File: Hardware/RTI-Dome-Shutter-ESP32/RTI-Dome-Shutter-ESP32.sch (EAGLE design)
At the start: 100 parts, among them IC1 REG1117FA-5.0_500, IC2 24LC64T-I/SN, IC8 REG1117-3.3V, J2 XT60PW-M, T1 MMBT3904LT1, T2 MMBT3904LT1, T3 MMBT3904LT1, U1 W5500, U2 ESP32-DevKitC ESP32-WROOM-32U, X9 J1011F01PNL

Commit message: Adding ESP32 version of the shutter controller
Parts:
- removed 25MHZ: CB3LV-OSCILATOR, rti:CB3LV-OSCILATOR
- removed C10: 22nF, rcl:C-EUC0603
- removed C11, C12, C14, C16, C17, C20: 100nF, rcl:C-EUC0603
- removed C13, C18, C22: 10nF, rcl:C-EUC0603
- removed C15, C21: 6.8nF, rcl:C-EUC0603
- removed C19: 4.7uF, rcl:C-EUC0603
- removed FL1: BLM21AG121SN1D, BLM21AG121SN1D:BLM21AG121SN1D
- removed R23: 10 1%, rcl:R-EU_R0603
- removed R24, R25, R26, R27: 49.9 1%, rcl:R-EU_R0603
- removed R28, R29: 330, rcl:R-EU_R0603
- removed R30, R31, R32, R33, R34, R35, R36, R37, R38, R40: 4.7K, rcl:R-EU_R0603
- removed R39: 12.4K 1%, rcl:R-EU_R0603
- removed U1: W5500, W5500:W5500
- removed X9: J1011F01PNL, rti:J1011F01PNL
- C1, C23, C24, C27, C28, C3, C4, C40, C41, C42, C43, C44, C45, C46, C5, C6: device rcl:C-EUC0603 -> rti:C-EU'0603'
- IC2: device Microchip_By_element14_Batch_1:24LC64T-I/SN -> rti:24LC64T-I/SN
- R1, R10, R12, R15, R16, R17, R18, R2, R20, R21, R22, R3, R4, R41, R44, R45, R46, R47, R48, R49, R5, R50, R6, R7, R8, R9: device rcl:R-EU_R0603 -> rti:R-EU'0603'
- T1, T2, T3: value MMBT3904LT1 -> (none); device samacsys:MMBT3904LT1 -> transistor:MMBT3904LT1-NPN-SOT23-BEC
- U2: value ESP32-DevKitC ESP32-WROOM-32U -> ESP32-DevKitC ESP32-WROOM-32D
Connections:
- removed net ACT_LED: U1.ACTLED, X9.C-L
- removed net AVDD: C11.1, C12.1, C14.1, C17.1, FL1.1, R23.2, R24.2, R25.2, U1.AVDD@1, U1.AVDD@2, U1.AVDD@3, U1.AVDD@4, U1.AVDD@5, U1.AVDD@6
- removed net LINK_ACK: U1.LINKLED, X9.C-R
- removed net N$10: R28.1, X9.AL
- removed net N$11: C15.2, X9.RD+
- removed net N$12: C21.2, X9.RD-
- removed net N$13: C10.1, R23.1, X9.CT
- removed net N$17: U1.DUPLED
- removed net N$22: R31.1, U1.RSVD@2
- removed net N$23: R32.1, U1.RSVD@3
- removed net N$24: R33.1, U1.RSVD@4
- removed net N$25: R34.1, U1.RSVD@5
- removed net N$26: R35.1, U1.RSVD@6
- removed net N$27: R36.1, U1.PMODE2
- removed net N$28: R37.1, U1.PMODE1
- removed net N$29: R38.1, U1.PMODE0
- removed net N$31: C19.2, U1.TOCAP
- removed net N$32: U1.VBG
- removed net N$33: C18.2, U1.1V2O
- removed net N$34: R39.1, U1.EXRES1
- removed net N$35: R40.2, U1.RSVD@1
- removed net N$7: C22.1, R26.2, R27.2, X9.CR
- removed net N$8: R29.1, X9.A-R
- removed net RXN: C21.1, R26.1, U1.RXN
- removed net RXP: C15.1, R27.1, U1.RXP
- removed net TXN: R25.1, U1.TXN, X9.TD-
- removed net TXP: R24.1, U1.TXP, X9.TD+
- removed net XI: 25MHZ.FO, U1.XI/CLKIN
- removed net XO: U1.XO
- net 3.3V: no longer 25MHZ.OE, 25MHZ.VDD, C13.1, C16.1, C20.1, FL1.2, R28.2, R29.2, R30.2, R36.2, R37.2, R38.2, U1.VDD
- net ETH_CS: no longer U1.SCS_N
- net ETH_RESET: no longer R30.1, U1.RST_N
- net GND: no longer 25MHZ.GND, C10.2, C11.2, C12.2, C13.2, C14.2, C16.2, C17.2, C18.1, C19.1, C20.2, C22.2, R31.2, R32.2, R33.2, R34.2, R35.2, R39.2, R40.1, U1.AGND@1, U1.AGND@2, U1.AGND@3, U1.AGND@4, U1.AGND@5, U1.AGND@6, U1.GND, X9.4/NC, X9.5/NC, X9.CGND, X9.CGND2
- net INT_N: no longer U1.INT_N
- net SCLK: no longer U1.SCLK
- net SDI: no longer U1.MISO
- net SDO: no longer U1.MOSI

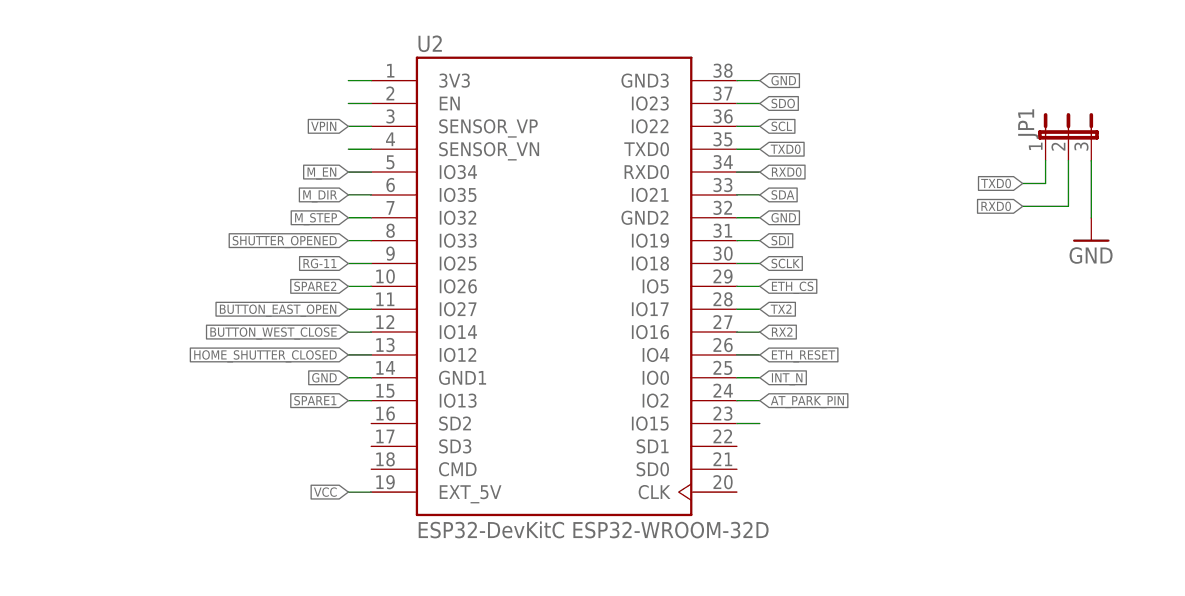
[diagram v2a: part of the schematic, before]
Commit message: Fixed a lot of issue with the ESP32 and serial ports.
Alpaca Discovery and API server are now running in their own tasks.
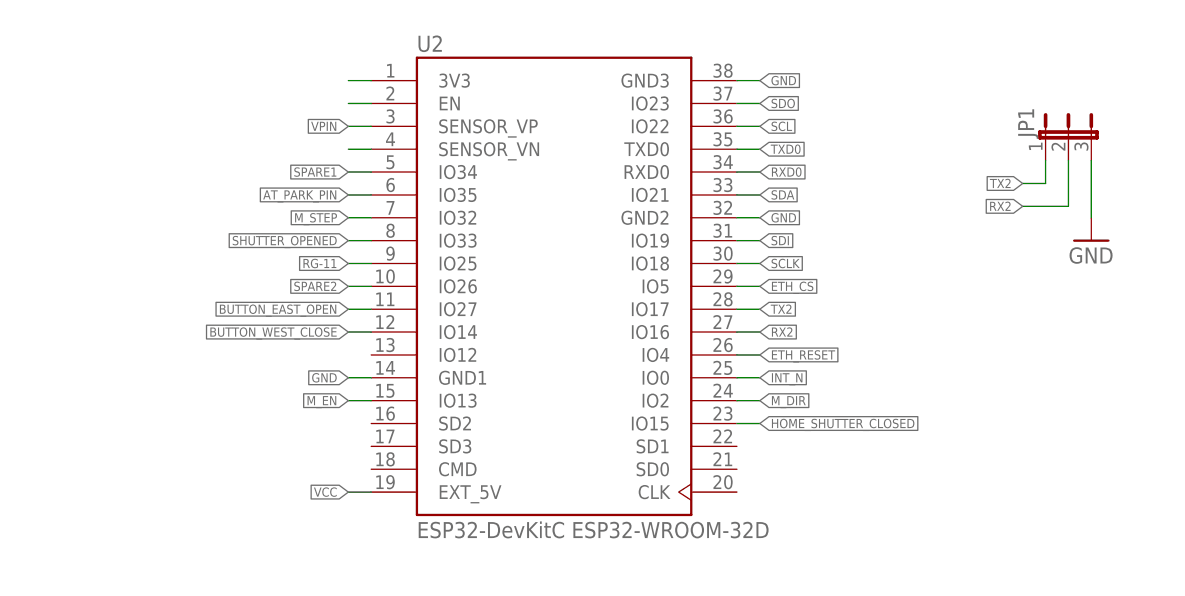
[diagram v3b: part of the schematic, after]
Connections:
- removed net N$15: U2.IO15
- net AT_PARK_PIN: now also U2.IO35; no longer U2.IO2
- net HOME_SHUTTER_CLOSED: now also U2.IO15; no longer U2.IO12
- net M_DIR: now also U2.IO2; no longer U2.IO35
- net M_EN: now also U2.IO13; no longer U2.IO34
- net RX2: now also JP1.2
- net RXD0: no longer JP1.2
- net SPARE1: now also U2.IO34; no longer U2.IO13
- net TX2: now also JP1.1
- net TXD0: no longer JP1.1
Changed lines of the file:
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@@
 </segment>
 <segment>
-<pinref part="U2" gate="G$1" pin="IO34"/>
-<wire x1="80.01" y1="67.31" x2="82.55" y2="67.31" width="0.1524" layer="91"/>
-<label x="80.01" y="67.31" size="1.016" layer="95" rot="R180" xref="yes"/>
+<wire x1="80.01" y1="41.91" x2="82.55" y2="41.91" width="0.1524" layer="91"/>
+<label x="80.01" y="41.91" size="1.016" layer="95" rot="R180" xref="yes"/>
+<pinref part="U2" gate="G$1" pin="IO13"/>
 </segment>
 </net>
@@
 </segment>
 <segment>
-<pinref part="U2" gate="G$1" pin="IO35"/>
-<wire x1="80.01" y1="64.77" x2="82.55" y2="64.77" width="0.1524" layer="91"/>
-<label x="80.01" y="64.77" size="1.016" layer="95" rot="R180" xref="yes"/>
+<wire x1="125.73" y1="41.91" x2="123.19" y2="41.91" width="0.1524" layer="91"/>
+<label x="125.73" y="41.91" size="1.016" layer="95" xref="yes"/>
+<pinref part="U2" gate="G$1" pin="IO2"/>
 </segment>
 </net>
@@
 </segment>
 <segment>
-<wire x1="80.01" y1="46.99" x2="82.55" y2="46.99" width="0.1524" layer="91"/>
-<label x="80.01" y="46.99" size="1.016" layer="95" rot="R180" xref="yes"/>
-<pinref part="U2" gate="G$1" pin="IO12"/>
+<pinref part="U2" gate="G$1" pin="IO15"/>
+<wire x1="125.73" y1="39.37" x2="123.19" y2="39.37" width="0.1524" layer="91"/>
+<label x="125.73" y="39.37" size="1.016" layer="95" xref="yes"/>
 </segment>
 </net>
@@
 </segment>
 <segment>
-<wire x1="125.73" y1="41.91" x2="123.19" y2="41.91" width="0.1524" layer="91"/>
-<label x="125.73" y="41.91" size="1.016" layer="95" xref="yes"/>
-<pinref part="U2" gate="G$1" pin="IO2"/>
+<pinref part="U2" gate="G$1" pin="IO35"/>
+<wire x1="80.01" y1="64.77" x2="82.55" y2="64.77" width="0.1524" layer="91"/>
+<label x="80.01" y="64.77" size="1.016" layer="95" rot="R180" xref="yes"/>
 </segment>
 </net>
@@
 <label x="125.73" y="49.53" size="1.016" layer="95" xref="yes"/>
 </segment>
+<segment>
+<pinref part="JP1" gate="1" pin="2"/>
+<wire x1="154.94" y1="63.5" x2="160.02" y2="63.5" width="0.1524" layer="91"/>
+<wire x1="160.02" y1="63.5" x2="160.02" y2="68.58" width="0.1524" layer="91"/>
+<label x="154.94" y="63.5" size="1.016" layer="95" ratio="4" rot="R180" xref="yes"/>
+</segment>
 </net>
 <net name="TX2" class="0">
@@
 <wire x1="125.73" y1="52.07" x2="123.19" y2="52.07" width="0.1524" layer="91"/>
 <label x="125.73" y="52.07" size="1.016" layer="95" xref="yes"/>
+</segment>
+<segment>
+<pinref part="JP1" gate="1" pin="1"/>
+<wire x1="154.94" y1="66.04" x2="157.48" y2="66.04" width="0.1524" layer="91"/>
+<wire x1="157.48" y1="66.04" x2="157.48" y2="68.58" width="0.1524" layer="91"/>
+<label x="154.94" y="66.04" size="1.016" layer="95" ratio="4" rot="R180" xref="yes"/>
 </segment>
 </net>
@@
 </segment>
 <segment>
-<wire x1="80.01" y1="41.91" x2="82.55" y2="41.91" width="0.1524" layer="91"/>
-<label x="80.01" y="41.91" size="1.016" layer="95" rot="R180" xref="yes"/>
-<pinref part="U2" gate="G$1" pin="IO13"/>
+<pinref part="U2" gate="G$1" pin="IO34"/>
+<wire x1="80.01" y1="67.31" x2="82.55" y2="67.31" width="0.1524" layer="91"/>
+<label x="80.01" y="67.31" size="1.016" layer="95" rot="R180" xref="yes"/>
 </segment>
 </net>
@@
 </segment>
 </net>
-<net name="N$15" class="0">
-<segment>
-<pinref part="U2" gate="G$1" pin="IO15"/>
-<wire x1="125.73" y1="39.37" x2="123.19" y2="39.37" width="0.1524" layer="91"/>
-</segment>
-</net>
 <net name="N$20" class="0">
 <segment>
@@
 <label x="125.73" y="69.85" size="1.016" layer="95" ratio="4" xref="yes"/>
 </segment>
-<segment>
-<pinref part="JP1" gate="1" pin="1"/>
-<wire x1="154.94" y1="66.04" x2="157.48" y2="66.04" width="0.1524" layer="91"/>
-<wire x1="157.48" y1="66.04" x2="157.48" y2="68.58" width="0.1524" layer="91"/>
-<label x="154.94" y="66.04" size="1.016" layer="95" ratio="4" rot="R180" xref="yes"/>
-</segment>
 </net>
 <net name="RXD0" class="0">
@@
 <label x="125.73" y="67.31" size="1.016" layer="95" ratio="4" xref="yes"/>
 </segment>
-<segment>
-<pinref part="JP1" gate="1" pin="2"/>
-<wire x1="154.94" y1="63.5" x2="160.02" y2="63.5" width="0.1524" layer="91"/>
-<wire x1="160.02" y1="63.5" x2="160.02" y2="68.58" width="0.1524" layer="91"/>
-<label x="154.94" y="63.5" size="1.016" layer="95" ratio="4" rot="R180" xref="yes"/>
-</segment>
-</net>
+</net>

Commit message: Latest board fixes with the extra output for lower shutter/other things.
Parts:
- removed U2: ESP32-DevKitC ESP32-WROOM-32D, ESP32-DEVKITC-32D:ESP32-DEVKITC-32D
- added U1: ESP32-DevKitC ESP32-WROOM-32U, ESP32-DEVKITC-32D:ESP32-DEVKITC-32D
- added X7: (no value), rti:AK500/3
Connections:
- removed net INT_N: U2.IO0
- removed net N$20: U2.3V3
- removed net N$21: U2.EN
- removed net N$36: U2.SENSOR_VN
- new net N$10: U1.EN
- new net N$11: U1.SENSOR_VN
- new net N$6: U$1G$1.Y5
- new net N$7: U$1G$1.Y6
- new net N$8: U$1G$1.Y7
- new net N$9: U1.3V3
- new net SPARE_OUT1: U$1G$1.A3, U1.IO0
- new net SPARE_OUT1_5V: U$1G$1.Y3, X7-3.KL
- new net SPARE_OUT2: U$1G$1.A4, U1.IO12
- new net SPARE_OUT2_5V: U$1G$1.Y4, X7-2.KL
- net AT_PARK_PIN: now also U1.IO35; no longer U2.IO35
- net BUTTON_EAST_OPEN: now also U1.IO27; no longer U2.IO27
- net BUTTON_WEST_CLOSE: now also U1.IO14; no longer U2.IO14
- net ETH_CS: now also U1.IO5; no longer U2.IO5
- net ETH_RESET: now also U1.IO4; no longer U2.IO4
- net GND: now also U1.GND1, U1.GND2, U1.GND3, X7-1.KL; no longer U$1G$1.A3, U$1G$1.A4, U2.GND1, U2.GND2, U2.GND3
- net HOME_SHUTTER_CLOSED: now also U1.IO15; no longer U2.IO15
- net M_DIR: now also U1.IO2; no longer U2.IO2
- net M_EN: now also U1.IO13; no longer U2.IO13
- net M_STEP: now also U1.IO32; no longer U2.IO32
- net RG-11: now also U1.IO25; no longer U2.IO25
- net RX2: now also U1.IO16; no longer U2.IO16
- net RXD0: now also U1.RXD0; no longer U2.RXD0
- net SCL: now also U1.IO22; no longer U2.IO22
- net SCLK: now also U1.IO18; no longer U2.IO18
- net SDA: now also U1.IO21; no longer U2.IO21
- net SDI: now also U1.IO19; no longer U2.IO19
- net SDO: now also U1.IO23; no longer U2.IO23
- net SHUTTER_OPENED: now also U1.IO33; no longer U2.IO33
- net SPARE1: now also U1.IO34; no longer U2.IO34
- net SPARE2: now also U1.IO26; no longer U2.IO26
- net TX2: now also U1.IO17; no longer U2.IO17
- net TXD0: now also U1.TXD0; no longer U2.TXD0
- net VCC: now also U1.EXT_5V; no longer U2.EXT_5V
- net VPIN: now also U1.SENSOR_VP; no longer U2.SENSOR_VP

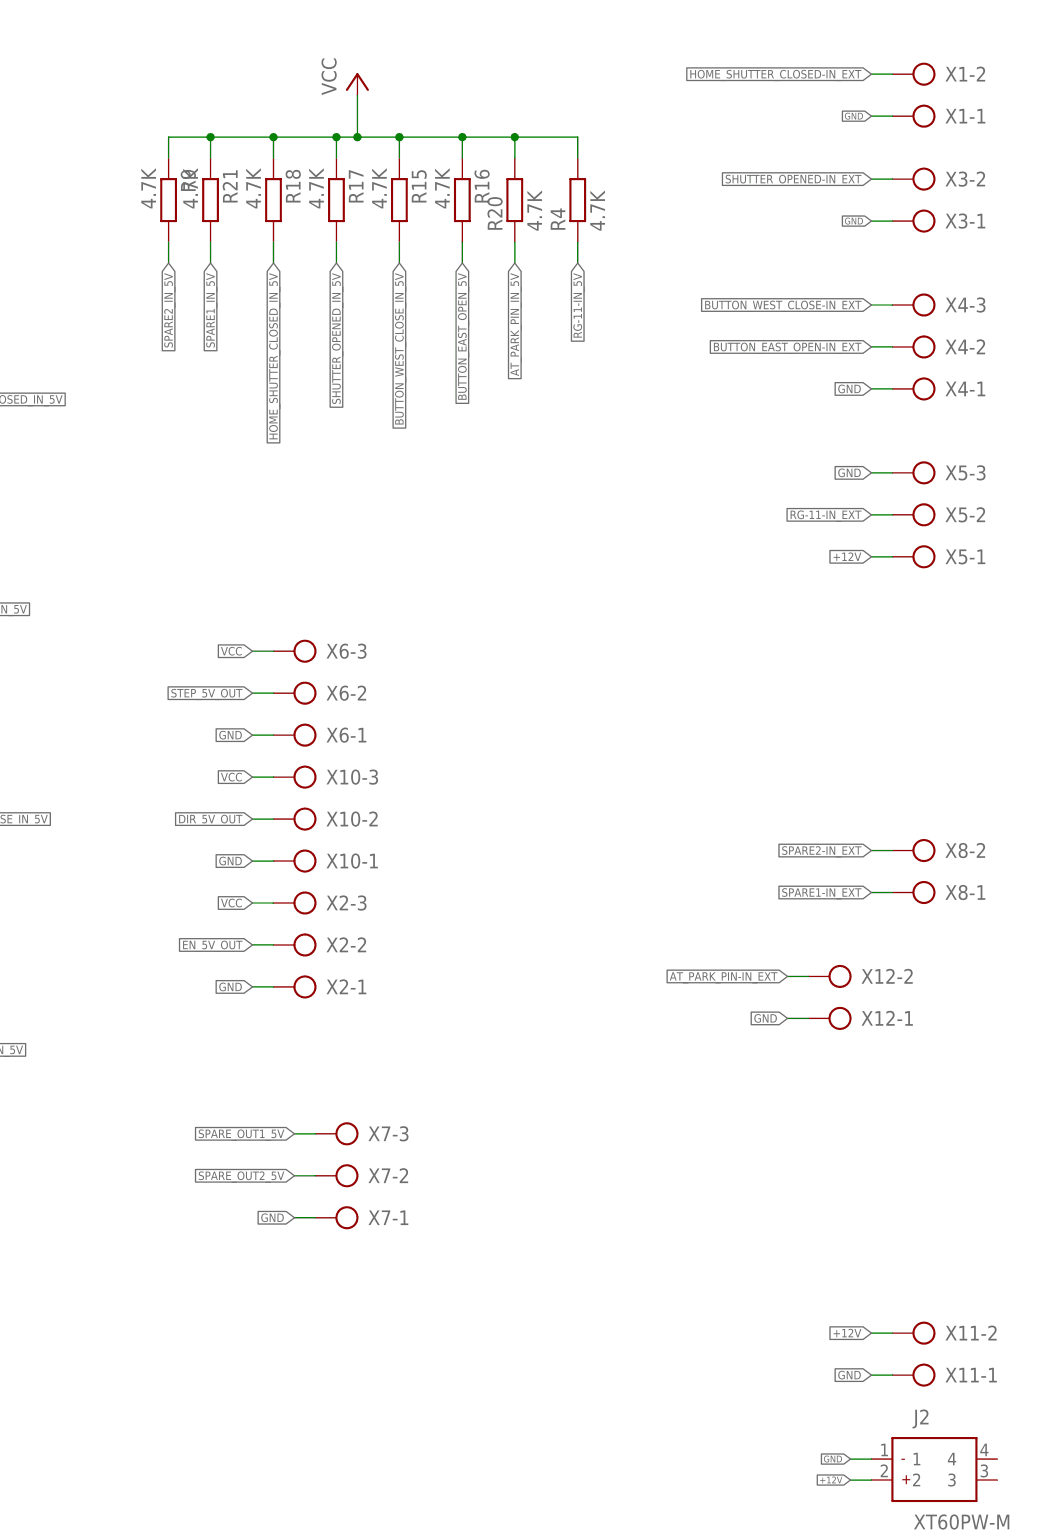
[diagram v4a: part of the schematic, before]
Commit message: Now using Wurth connector for rotator and shutter.
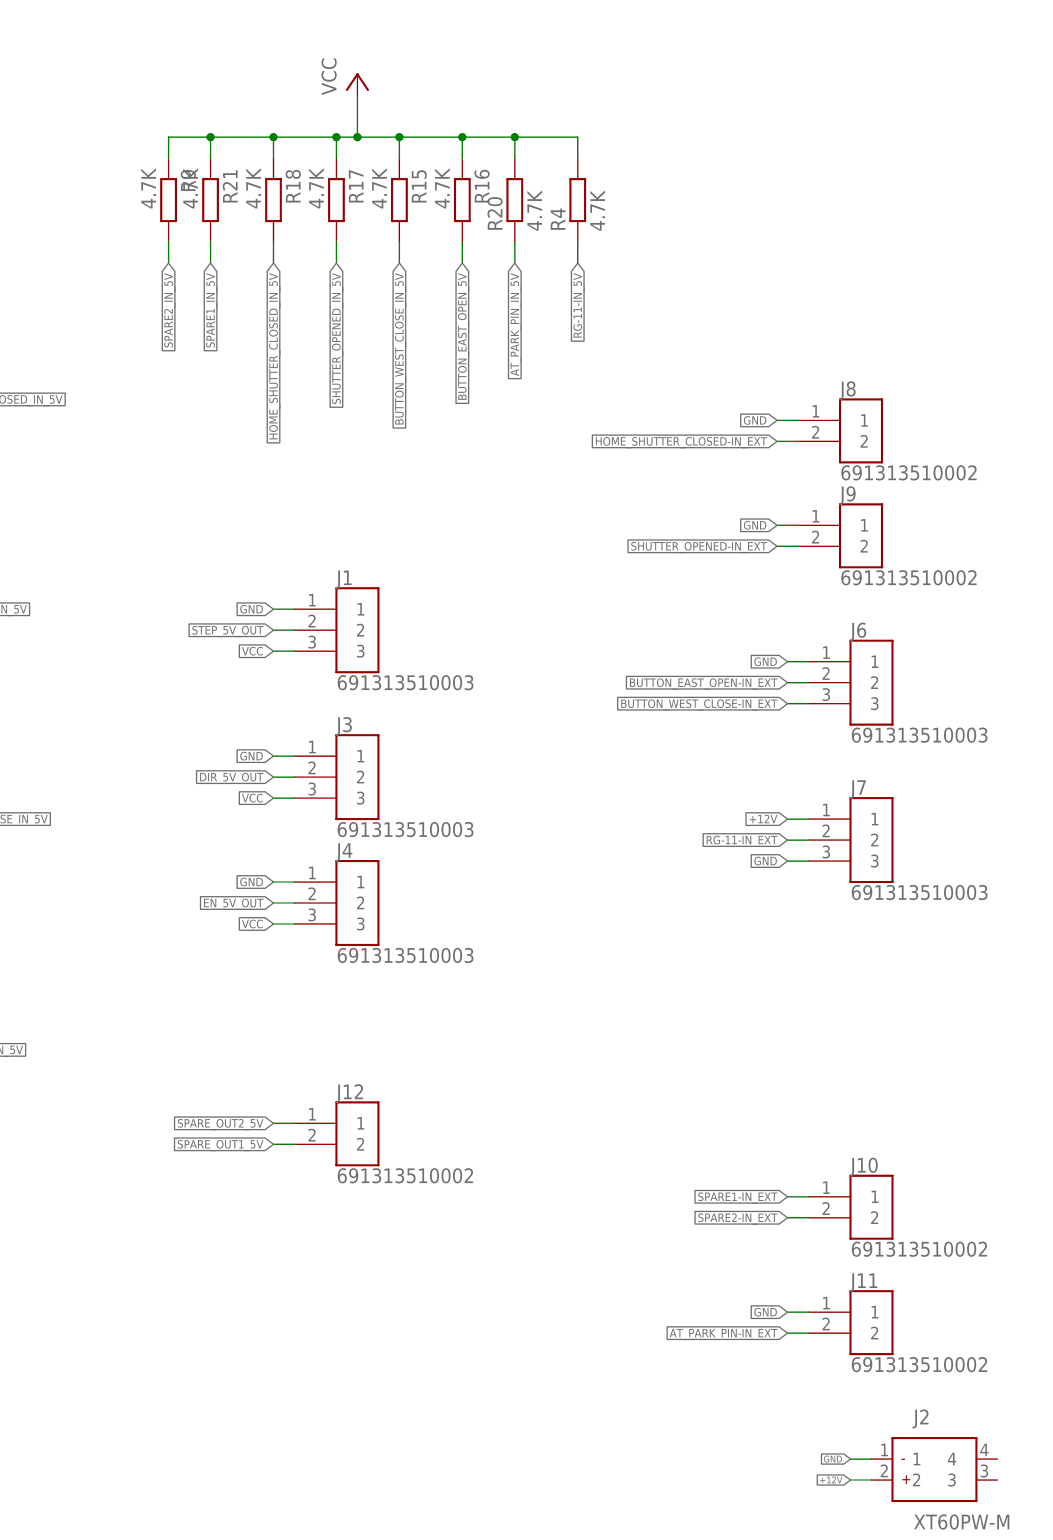
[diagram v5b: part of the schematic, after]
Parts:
- removed X1, X11, X12, X3, X8: (no value), rti:AK500/2
- removed X10, X2, X4, X5, X6, X7: (no value), rti:AK500/3
- added J1, J3, J4, J6, J7: 691313510003, samacsys:691313510003
- added J10, J11, J12, J8, J9: 691313510002, samacsys:691313510002
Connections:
- net +12V: now also J7.1; no longer X11-2.KL, X5-1.KL
- net AT_PARK_PIN-IN_EXT: now also J11.2; no longer X12-2.KL
- net BUTTON_EAST_OPEN-IN_EXT: now also J6.2; no longer X4-2.KL
- net BUTTON_WEST_CLOSE-IN_EXT: now also J6.3; no longer X4-3.KL
- net DIR_5V_OUT: now also J3.2; no longer X10-2.KL
- net EN_5V_OUT: now also J4.2; no longer X2-2.KL
- net GND: now also J1.1, J11.1, J3.1, J4.1, J6.1, J7.3, J8.1, J9.1; no longer X1-1.KL, X10-1.KL, X11-1.KL, X12-1.KL, X2-1.KL, X3-1.KL, X4-1.KL, X5-3.KL, X6-1.KL, X7-1.KL
- net HOME_SHUTTER_CLOSED-IN_EXT: now also J8.2; no longer X1-2.KL
- net RG-11-IN_EXT: now also J7.2; no longer X5-2.KL
- net SHUTTER_OPENED-IN_EXT: now also J9.2; no longer X3-2.KL
- net SPARE1-IN_EXT: now also J10.1; no longer X8-1.KL
- net SPARE2-IN_EXT: now also J10.2; no longer X8-2.KL
- net SPARE_OUT1_5V: now also J12.2; no longer X7-3.KL
- net SPARE_OUT2_5V: now also J12.1; no longer X7-2.KL
- net STEP_5V_OUT: now also J1.2; no longer X6-2.KL
- net VCC: now also J1.3, J3.3, J4.3; no longer X10-3.KL, X2-3.KL, X6-3.KL
